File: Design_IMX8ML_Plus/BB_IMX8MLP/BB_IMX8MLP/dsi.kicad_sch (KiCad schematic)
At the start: 11 parts, among them J15 DSI, U21 D3V3F4U10LP-7, U29 D3V3F4U10LP-7, U52 FXMA2102L8X

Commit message: [LoRa] Starting a new project
Starting a new project base on LoRa LR1121, this project use
the module LBAA0XV2GT-001 that had sub-GHz and 2.4GHz frequencies.
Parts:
- U28: value ~ -> D3V3F4U10LP-7; MP (none) -> D3V3F4U10LP-7; Price (none) -> 0.35
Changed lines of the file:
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@@
 			)
 		)
-		(property "Value" "~"
+		(property "Value" "D3V3F4U10LP-7"
 			(at 126.365 152.4 0)
 			(effects
@@
 			(at 127 157.48 0)
 			(effects
+				(font
+					(size 1.27 1.27)
+				)
+				(hide yes)
+			)
+		)
+		(property "MP" "D3V3F4U10LP-7"
+			(at 127 157.48 0)
+			(effects
+				(font
+					(size 1.27 1.27)
+				)
+				(hide yes)
+			)
+		)
+		(property "Price" "0.35"
+			(at 127 157.48 0)
+			(effects

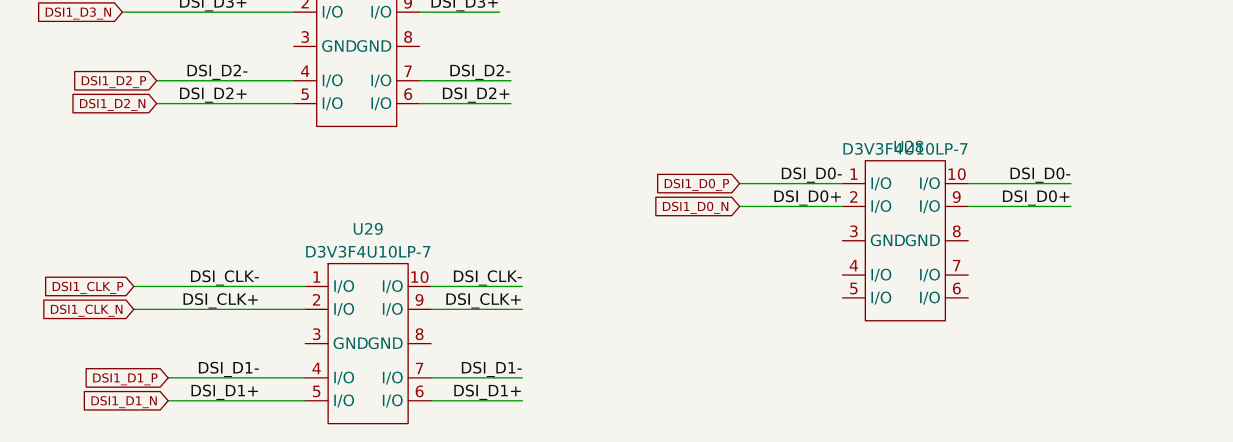
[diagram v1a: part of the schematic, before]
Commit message: [BB_IMX8ML] It was reoganizated the device position
It was reorganized the devices to improve the routing.
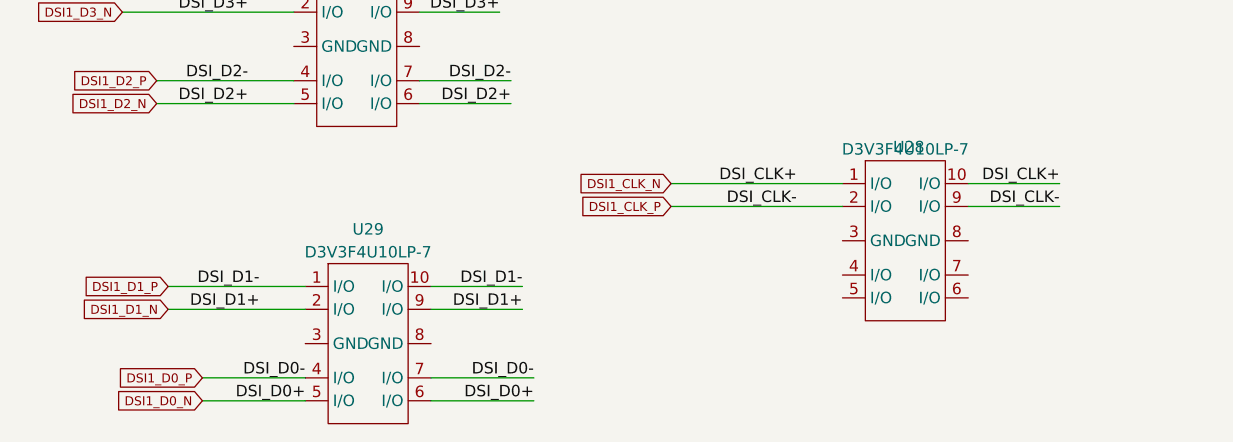
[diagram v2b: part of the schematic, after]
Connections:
- net DSI1_CLK_N: now also U28.1 (I/O), U28.10 (I/O); no longer U29.2 (I/O), U29.9 (I/O)
- net DSI1_CLK_P: now also U28.2 (I/O), U28.9 (I/O); no longer U29.1 (I/O), U29.10 (I/O)
- net DSI1_D0_N: now also U29.5 (I/O), U29.6 (I/O); no longer U28.2 (I/O), U28.9 (I/O)
- net DSI1_D0_P: now also U29.4 (I/O), U29.7 (I/O); no longer U28.1 (I/O), U28.10 (I/O)
- net DSI1_D1_N: now also U29.2 (I/O), U29.9 (I/O); no longer U29.5 (I/O), U29.6 (I/O)
- net DSI1_D1_P: now also U29.1 (I/O), U29.10 (I/O); no longer U29.4 (I/O), U29.7 (I/O)
